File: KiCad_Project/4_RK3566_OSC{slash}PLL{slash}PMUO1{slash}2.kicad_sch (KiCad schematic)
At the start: 27 parts, among them X1 XL2EL89COI-111YLC-24M

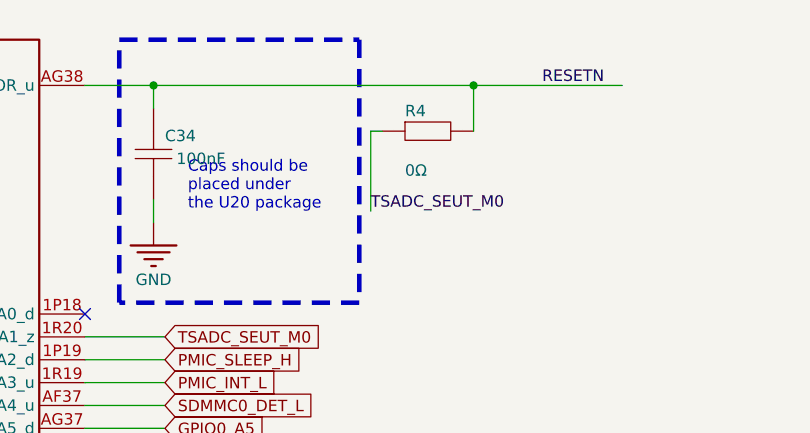
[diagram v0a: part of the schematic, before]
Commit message: Update additional PCBs
Add WIFI PCB to get best antenna
Add Display Debbugger to get interface pinout
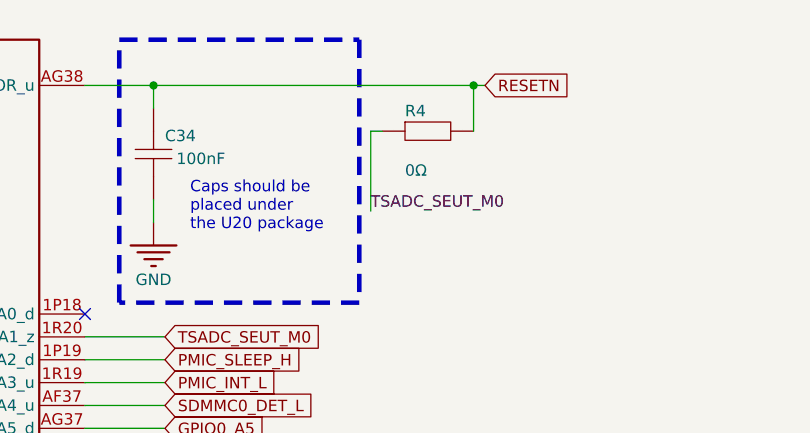
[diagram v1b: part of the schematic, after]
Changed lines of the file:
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@@
 	(text "Caps should be \nplaced under \nthe U20 package"
 		(exclude_from_sim no)
-		(at 252.73 57.15 0)
+		(at 252.984 59.436 0)
 		(effects
 			(font
@@
 	(wire
 		(pts
-			(xy 300.99 43.18) (xy 284.48 43.18)
+			(xy 285.75 43.18) (xy 284.48 43.18)
 		)
 		(stroke
@@
 			(width 0)
 			(type default)
-		)
-	)
-	(label "RESETN"
-		(at 292.1 43.18 0)
-		(effects
-			(font
-				(size 1.27 1.27)
-			)
-			(justify left bottom)
 		)
 	)
@@
 			(effects
 				(font
+					(size 1.27 1.27)
+				)
+				(justify left)
+				(hide yes)
+			)
+		)
+	)
+	(global_label "RESETN"
+		(shape input)
+		(at 285.75 43.18 0)
+		(fields_autoplaced yes)
+		(effects
+			(font
+				(size 1.27 1.27)
+			)
+			(justify left)
+		)
+		(property "Intersheetrefs" "${INTERSHEET_REFS}"
+			(at 295.8108 43.18 0)
+			(effects
+				(font
